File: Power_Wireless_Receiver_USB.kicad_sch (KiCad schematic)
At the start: 29 parts, among them J601 USB_C_Receptacle_PowerOnly_6P, J602 Solder Pad, J603 Solder Pad, Q601 CSD75207W15, U601 BQ51013CQWRHLRQ1

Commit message: Added footprints, images, almost finished all èages except for the MCU
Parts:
- removed C602: 100n X7R 16V, Capacitor_SMD:C_0402_1005Metric, symbol Device:C_Small
- removed C609: 47n X7R 16V, symbol Device:C_Small
- removed C610: 470n X7R 16V, symbol Device:C_Small
- removed C612: 10n X7R 16V, symbol Device:C_Small
- removed C617: 1u X7R 16V, Capacitor_SMD:C_0603_1608Metric, symbol Device:C_Small
- removed NT601: NetTie_2, symbol Device:NetTie_2
- removed R604, R605, R606: 330R 1%, symbol Device:R_Small
- added C1004: 10u X5R 16V, Capacitor_SMD:C_0603_1608Metric, symbol Device:C_Small
- added C613: 22n X7R 25V, Capacitor_SMD:C_0402_1005Metric, symbol Device:C_Small
- added C615, C616: 10n C0G 25V, Capacitor_SMD:C_0402_1005Metric, symbol Device:C_Small
- added C704: 1u X7R 16V, Capacitor_SMD:C_0603_1608Metric, symbol Device:C_Small
- added TP506: +VBUS, 0_Zenith:TestPoint_Pad_D0.5mm_Front, symbol Connector:TestPoint
- added TP507: ~{AD_EN}, 0_Zenith:TestPoint_Pad_D0.5mm_Front, symbol Connector:TestPoint
- added TP508: ~{CHG}, 0_Zenith:TestPoint_Pad_D0.5mm_Front, symbol Connector:TestPoint
- added TP509: +VCHARGE, 0_Zenith:TestPoint_Pad_D0.5mm_Front, symbol Connector:TestPoint
- C605: value 470n X7R 16V -> 470n X7R 25V; footprint (none) -> Capacitor_SMD:C_0603_1608Metric; Manufacturer (none) -> Murata Electronics; Manufacturer Part Number (none) -> GCM188R71E474KA64D; Supplier (none) -> Mouser Electronics; Supplier Part Number (none) -> 81-GCM188R71E474KA4D
- C606, C608: value 47n X7R 16V -> 470n X7R 25V; footprint (none) -> Capacitor_SMD:C_0603_1608Metric; Manufacturer (none) -> Murata Electronics; Manufacturer Part Number (none) -> GCM188R71E474KA64D; Supplier (none) -> Mouser Electronics; Supplier Part Number (none) -> 81-GCM188R71E474KA4D
- C607: value 10n X7R 16V -> 470n X7R 25V; footprint (none) -> Capacitor_SMD:C_0603_1608Metric; Manufacturer (none) -> Murata Electronics; Manufacturer Part Number (none) -> GCM188R71E474KA64D; Supplier (none) -> Mouser Electronics; Supplier Part Number (none) -> 81-GCM188R71E474KA4D
- C612: renamed from C611; value 47n X7R 16V -> 22n X7R 25V; footprint (none) -> Capacitor_SMD:C_0402_1005Metric; Manufacturer (none) -> Murata Electronics; Manufacturer Part Number (none) -> GCM155R71E223KA55D; Supplier (none) -> Mouser Electronics; Supplier Part Number (none) -> 81-GCM155R71E223KA5D
- D601: footprint (none) -> 0_Plume:D_SOD-123FL
- J601: footprint (none) -> 0_Plume:USB4125-GF-A; Manufacturer (none) -> GCT; Manufacturer Part Number (none) -> USB4125-GF-A; Supplier (none) -> Mouser Electronics; Supplier Part Number (none) -> 640-USB4125-GF-A
- LED601: footprint Charge_Manager_FP:KingBright_LED_0805 -> 0_Plume:Bivar_LED_0603; Manufacturer Kingbright -> Bivar; Manufacturer Part Number AP2012MGC -> SM0603SRC; Supplier Part Number 604-AP2012MGC -> 749-SM0603SRC
- Q601: footprint (none) -> 0_Plume:Texas_DSBGA-9_1.62x1.58mm_Layout3x3_P0.5mm; Manufacturer (none) -> Texas Instruments; Manufacturer Part Number (none) -> CSD75207W15; Supplier (none) -> Mouser Electronics; Supplier Part Number (none) -> 595-CSD75207W15
- R601: footprint (none) -> Resistor_SMD:R_0402_1005Metric; Manufacturer (none) -> KOA Speer; Manufacturer Part Number (none) -> RK73H1ETTP3300F; Supplier (none) -> Mouser Electronics; Supplier Part Number (none) -> 660-RK73H1ETTP3300F
- R602, R603: Manufacturer Vishay / Dale -> KOA Speer; Manufacturer Part Number RCS04025K10FKED -> RK73H1ETTP5101F; Supplier Part Number 71-RCS04025K10FKED -> 660-RK73H1ETTP5101F
- U601: footprint Package_DFN_QFN:Texas_VQFN-RHL-20 -> 0_Plume:BQ51013CQWRHLRQ1; Manufacturer (none) -> Texas Instruments; Manufacturer Part Number (none) -> BQ51013CQWRHLRQ1; Supplier (none) -> Mouser Electronics; Supplier Part Number (none) -> 595-BQ51013CQWRHLRQ1
- renumbered C613 to C614
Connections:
- net AD is gone; now on net +VBUS: U601.9 (AD)
- net +VBUS: now also C704.1, TP506.1
- net +VCHARGE: now also C601.1, C1004.1, TP509.1
- net GND: now also C601.2, C1004.2, C704.2; no longer U601.11 (EN2)
- net ~{AD_EN}: now also TP507.1
- net ~{CHG}: now also TP508.1
- net FOD: now reaches U601.14 (FOD)
- net RECT: now reaches C614.1, U601.18 (RECT)
- net CLAMP1: now reaches C605.1, U601.5 (CLAMP1)
- net AC1: now reaches C605.2, C608.2, U601.2 (AC1)
- net AC1: now also C607.1, C613.2, C616.2; no longer C606.2, C607.2
- net AC2: now reaches C612.1, J603.1, U601.19 (AC2)
- net AC2: now also C606.1, C607.2, C615.1
- net COMM2: now reaches C612.2, U601.15 (COMM2)
- net TS/CTRL: now reaches TH601.1, U601.13 (TS/CTRL)
- net BOOT2: now reaches U601.17 (BOOT2)
- net BOOT2: now also C615.2
- net ILIM: now reaches U601.12 (ILIM)
- net CLAMP2: now reaches U601.16 (CLAMP2)
- net CLAMP2: now also C606.2
- net BOOT1: now reaches U601.3 (BOOT1)
- net BOOT1: now also C616.1; no longer C607.1
- net COMM1: now reaches U601.6 (COMM1)
- net COMM1: now also C613.1; no longer C606.1
- new net EN1: U601.10 (TERM)
- new net EN2: U601.11 (EN2)
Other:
- note added: "DSBGA-9 1.5x1.5 mm"
- note added: "EN1 and EN2 have internal pulldown resistors."
- note added: "VQFN-20 4.5x3.5mm"
- moved on the sheet: C601, C603, C604, C605, C612, C614, D601, J601, J602, J603, LED601, Q601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

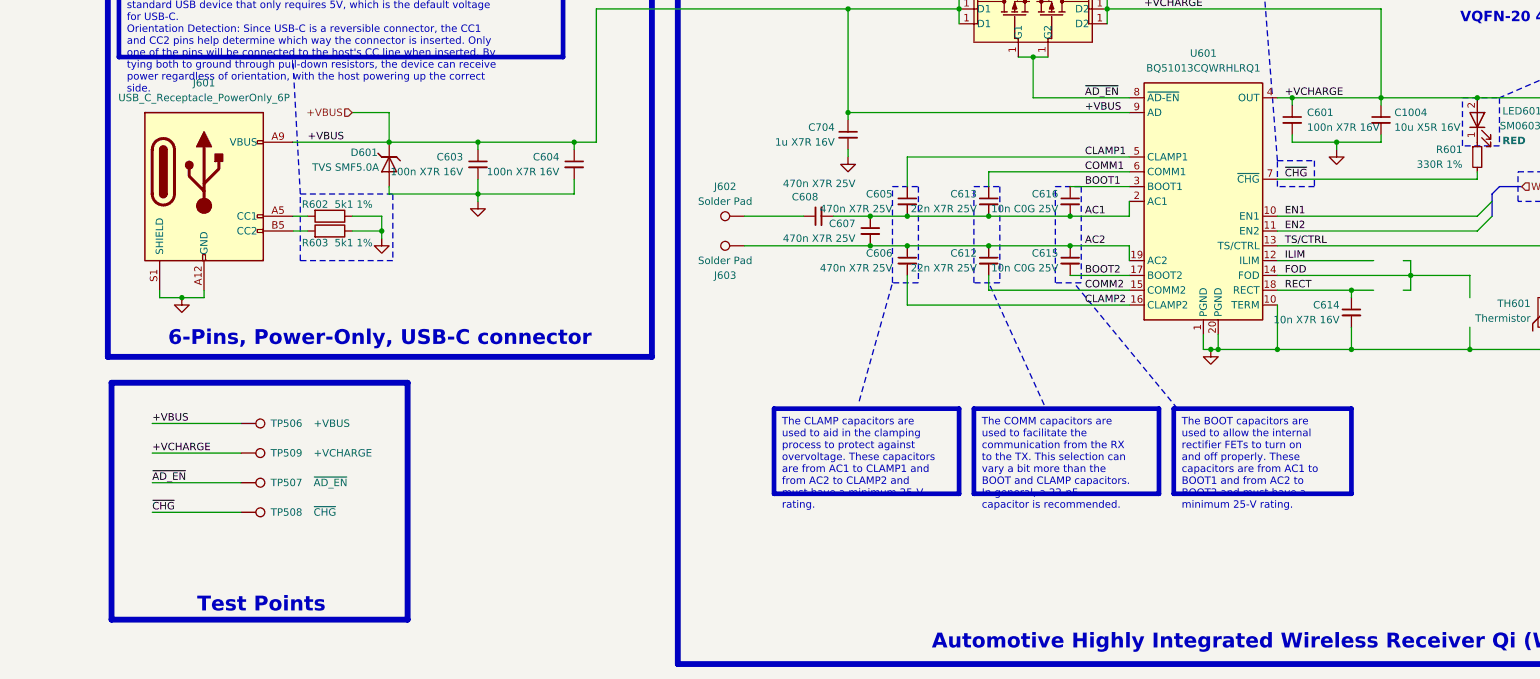
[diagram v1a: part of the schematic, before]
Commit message: Added RGB LED, added motor connectors, added test points, imported all 3D models
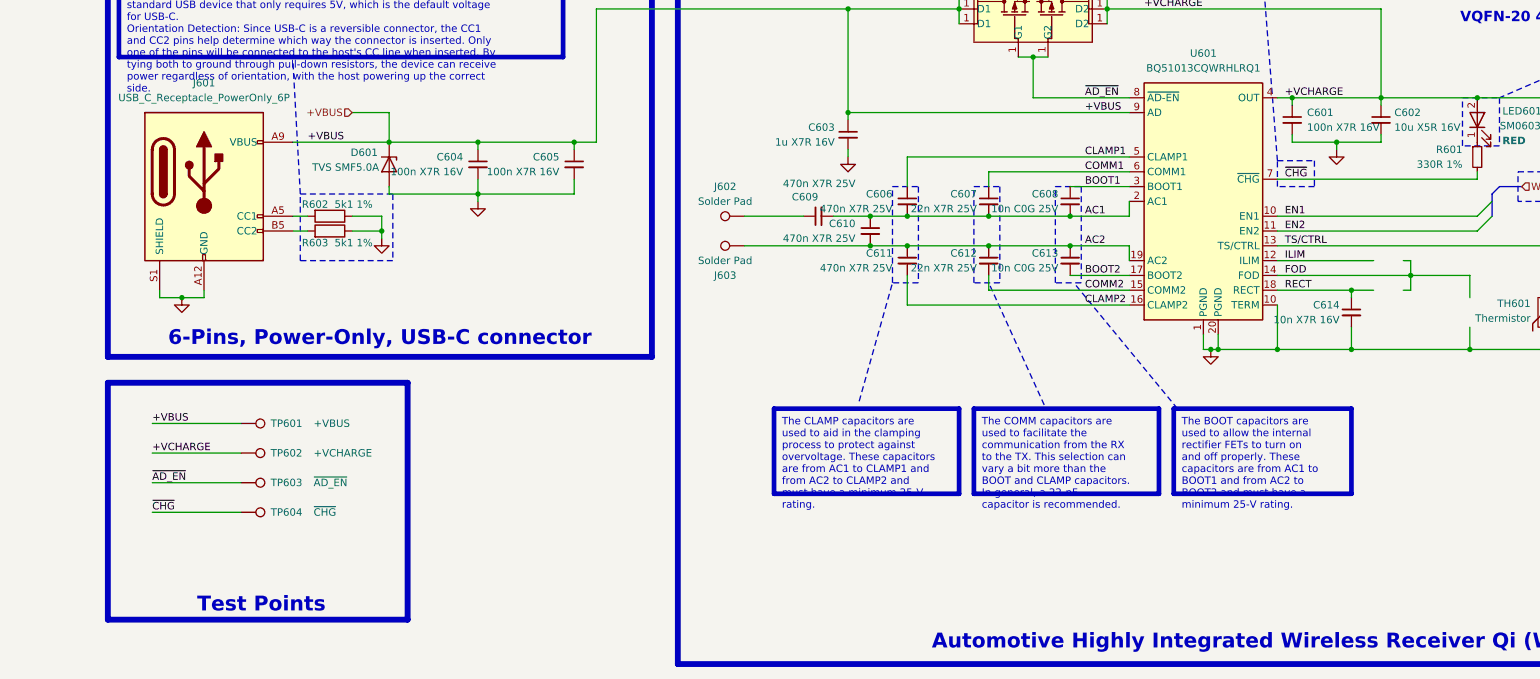
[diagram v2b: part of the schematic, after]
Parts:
- TP601: renamed from TP506; footprint 0_Zenith:TestPoint_Pad_D0.5mm_Front -> 0_Plume:TestPoint_Pad_D0.5mm_Back
- TP602: renamed from TP509; footprint 0_Zenith:TestPoint_Pad_D0.5mm_Front -> 0_Plume:TestPoint_Pad_D0.5mm_Back
- TP603: renamed from TP507; footprint 0_Zenith:TestPoint_Pad_D0.5mm_Front -> 0_Plume:TestPoint_Pad_D0.5mm_Back
- TP604: renamed from TP508; footprint 0_Zenith:TestPoint_Pad_D0.5mm_Front -> 0_Plume:TestPoint_Pad_D0.5mm_Back
- renumbered C1004 to C602, C704 to C603, C603 to C604, C604 to C605, C605 to C606, C613 to C607, C616 to C608, C608 to C609, C607 to C610, C606 to C611, C615 to C613
